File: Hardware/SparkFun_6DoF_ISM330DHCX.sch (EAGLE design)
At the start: 31 parts, among them J1 QWIIC_RIGHT_ANGLE, J2 QWIIC_RIGHT_ANGLE, U1 ISM330DHCX

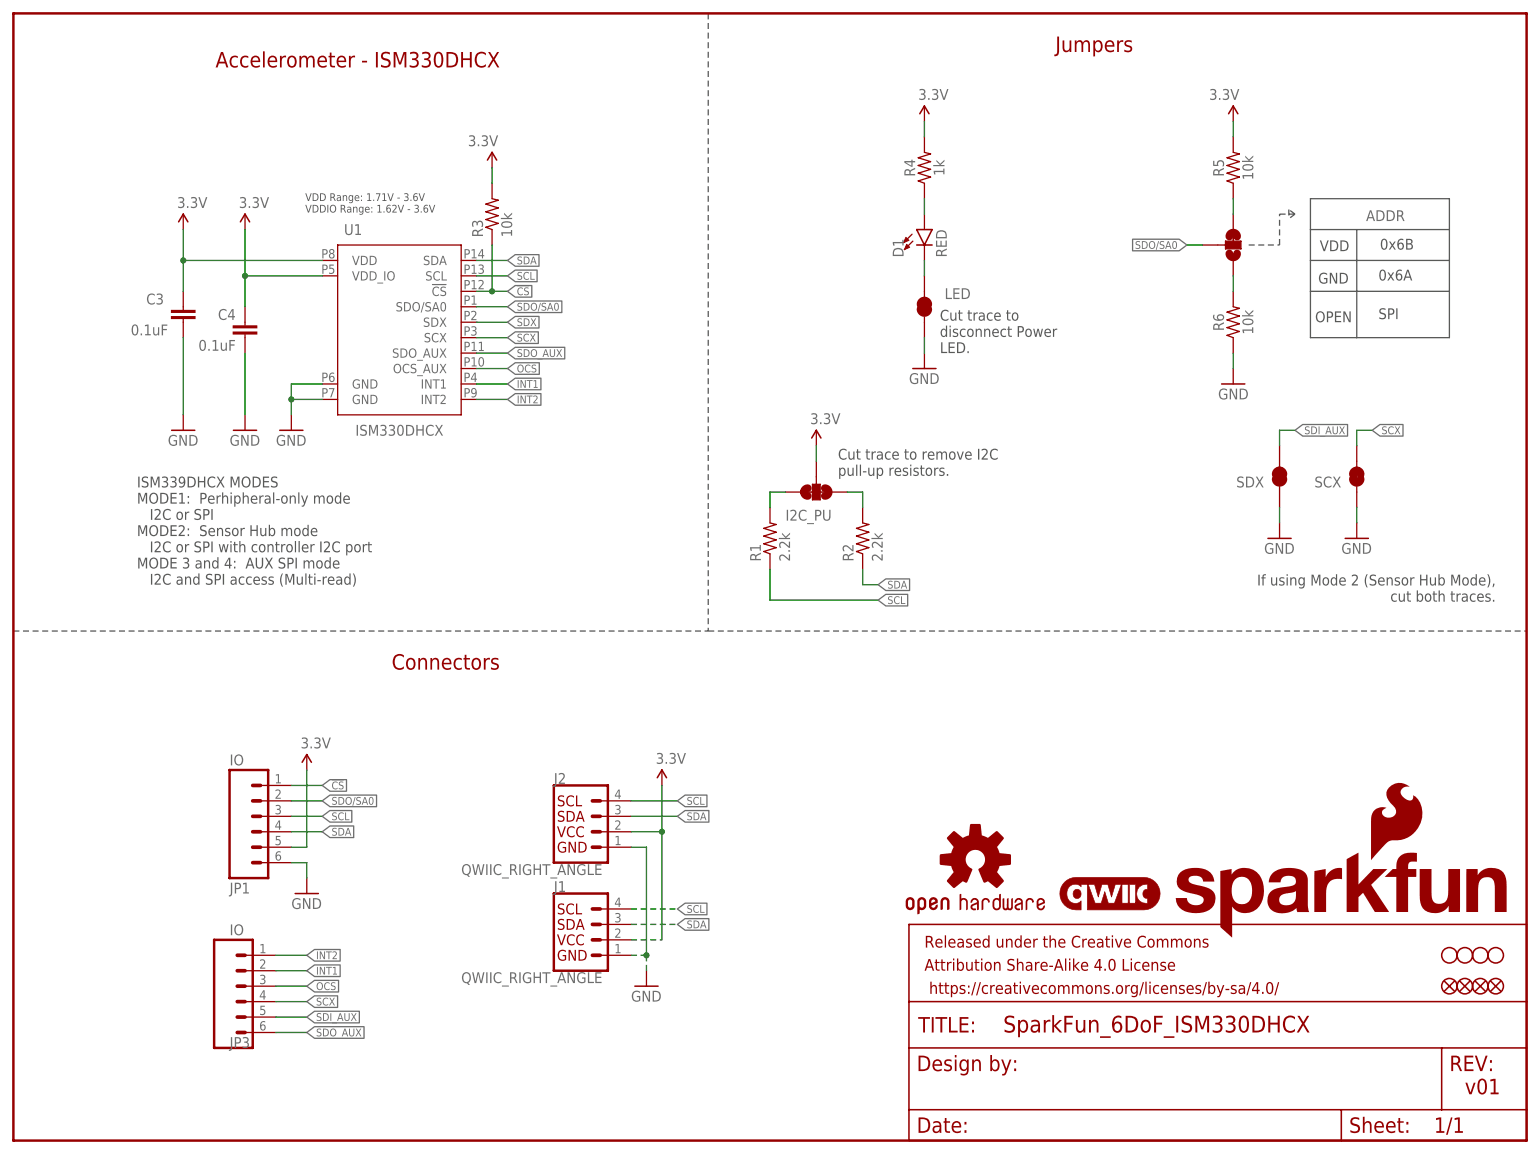
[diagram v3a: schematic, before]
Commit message: Completes routing, had to swap SDO and CS for ease of routing
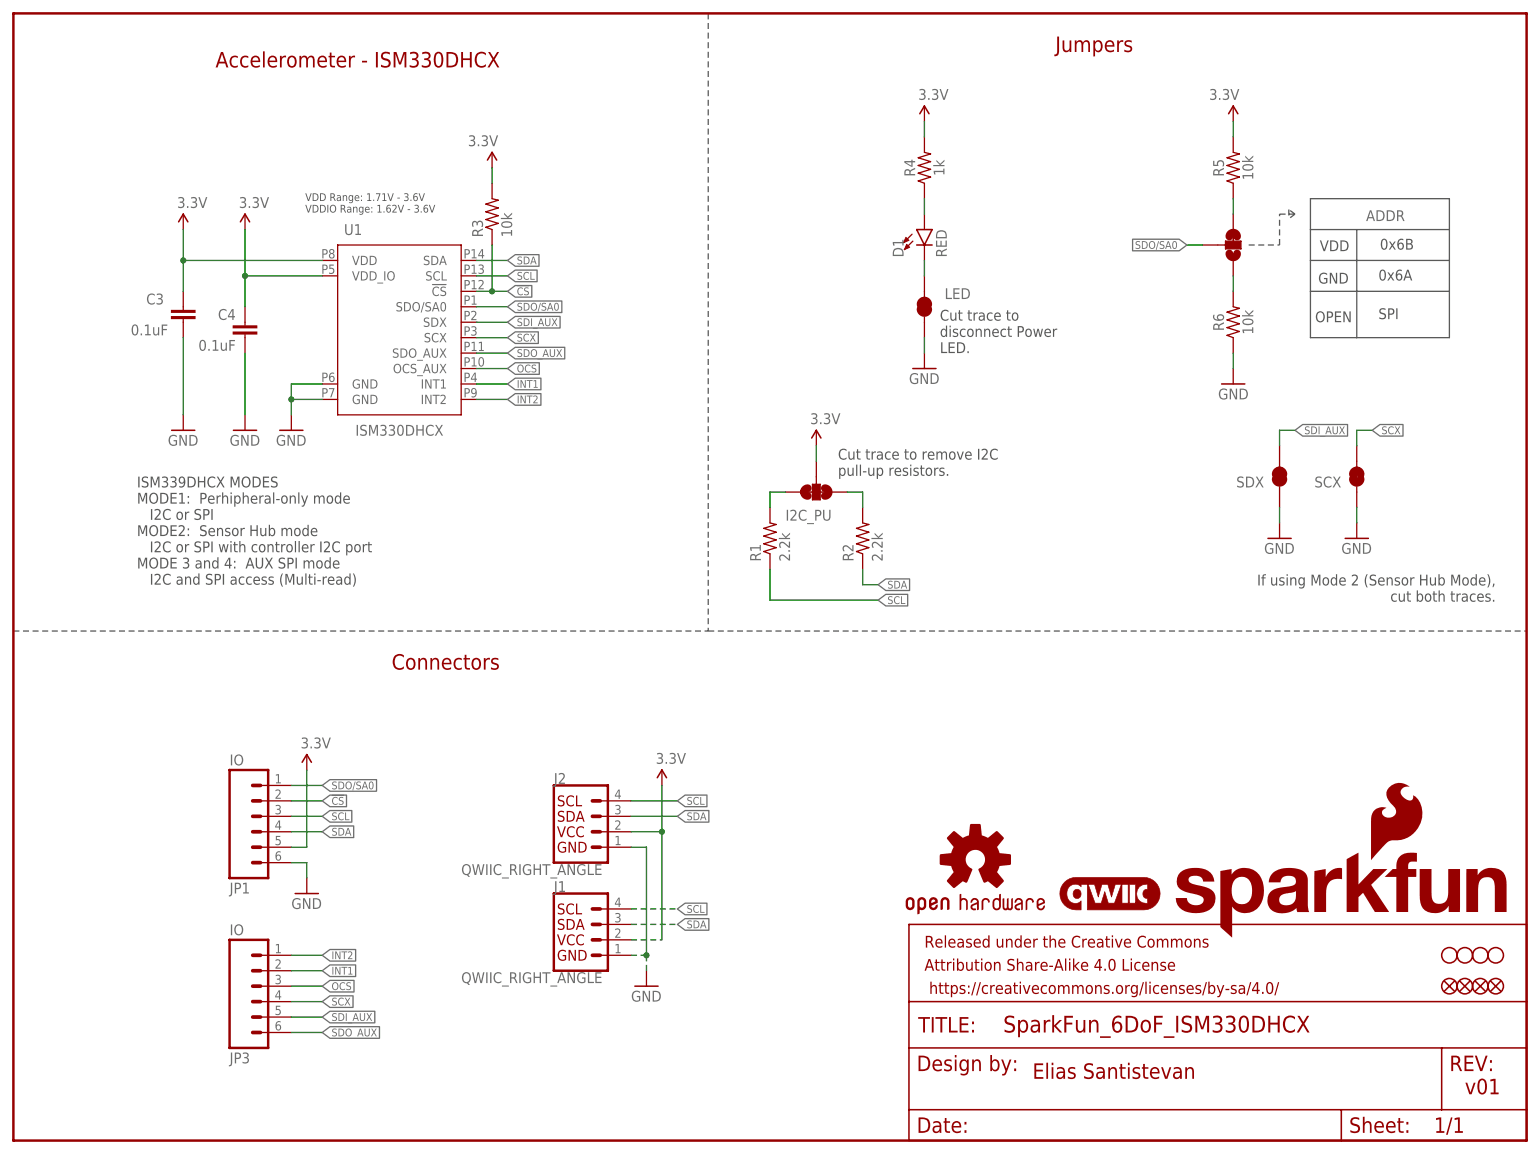
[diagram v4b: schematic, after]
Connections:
- removed net N$4: C3.1, U1.VDD
- removed net SDX: U1.SDX
- net !CS!: now also JP1.2; no longer JP1.1
- net 3.3V: now also C3.1, U1.VDD
- net SDI_AUX: now also U1.SDX
- net SDO/SA0: now also JP1.1; no longer JP1.2
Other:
- note added: "Elias Santistevan"
- moved on the sheet: JP3
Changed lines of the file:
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@@
 <wire x1="209.804" y1="153.162" x2="209.804" y2="151.638" width="0.2032" layer="97" style="dashdot"/>
 <wire x1="210.82" y1="152.4" x2="209.804" y2="151.638" width="0.2032" layer="97" style="dashdot"/>
+<text x="167.64" y="10.16" size="2.54" layer="94" font="vector">Elias Santistevan</text>
 </plain>
 <instances>
@@
 </instance>
 <instance part="LOGO3" gate="G$1" x="190.5" y="33.02" smashed="yes"/>
-<instance part="JP3" gate="G$1" x="38.1" y="25.4" smashed="yes" rot="MR180">
+<instance part="JP3" gate="G$1" x="40.64" y="25.4" smashed="yes" rot="MR180">
 <attribute name="VALUE" x="35.56" y="35.56" size="1.778" layer="96" font="vector" rot="MR180"/>
-<attribute name="NAME" x="35.56" y="17.018" size="1.778" layer="95" font="vector" rot="MR180"/>
+<attribute name="NAME" x="35.56" y="14.478" size="1.778" layer="95" font="vector" rot="MR180"/>
 </instance>
 <instance part="J1" gate="G$1" x="93.98" y="33.02" smashed="yes">
@@
 </segment>
 <segment>
-<pinref part="JP1" gate="G$1" pin="1"/>
-<wire x1="45.72" y1="58.42" x2="50.8" y2="58.42" width="0.1524" layer="91"/>
-<label x="50.8" y="58.42" size="1.27" layer="95" font="vector" xref="yes"/>
-</segment>
-</net>
-<net name="SDO/SA0" class="0">
-<segment>
-<pinref part="JP1" gate="G$1" pin="2"/>
 <wire x1="45.72" y1="55.88" x2="50.8" y2="55.88" width="0.1524" layer="91"/>
 <label x="50.8" y="55.88" size="1.27" layer="95" font="vector" xref="yes"/>
-</segment>
+<pinref part="JP1" gate="G$1" pin="2"/>
+</segment>
+</net>
+<net name="SDO/SA0" class="0">
 <segment>
 <wire x1="76.2" y1="137.16" x2="81.28" y2="137.16" width="0.1524" layer="91"/>
@@
 <label x="193.04" y="147.32" size="1.27" layer="95" font="vector" rot="R180" xref="yes"/>
 </segment>
+<segment>
+<wire x1="45.72" y1="58.42" x2="50.8" y2="58.42" width="0.1524" layer="91"/>
+<label x="50.8" y="58.42" size="1.27" layer="95" font="vector" xref="yes"/>
+<pinref part="JP1" gate="G$1" pin="1"/>
+</segment>
 </net>
 <net name="SDI_AUX" class="0">
 <segment>
 <pinref part="JP3" gate="G$1" pin="5"/>
-<wire x1="43.18" y1="20.32" x2="48.26" y2="20.32" width="0.1524" layer="91"/>
-<label x="48.26" y="20.32" size="1.27" layer="95" font="vector" xref="yes"/>
+<wire x1="45.72" y1="20.32" x2="50.8" y2="20.32" width="0.1524" layer="91"/>
+<label x="50.8" y="20.32" size="1.27" layer="95" font="vector" xref="yes"/>
 </segment>
 <segment>
@@
 <label x="210.82" y="116.84" size="1.27" layer="95" font="vector" xref="yes"/>
 </segment>
+<segment>
+<wire x1="76.2" y1="134.62" x2="81.28" y2="134.62" width="0.1524" layer="91"/>
+<label x="81.28" y="134.62" size="1.27" layer="95" font="vector" xref="yes"/>
+<pinref part="U1" gate="G$1" pin="SDX"/>
+</segment>
 </net>
 <net name="SCX" class="0">
 <segment>
 <pinref part="JP3" gate="G$1" pin="4"/>
-<wire x1="43.18" y1="22.86" x2="48.26" y2="22.86" width="0.1524" layer="91"/>
-<label x="48.26" y="22.86" size="1.27" layer="95" font="vector" xref="yes"/>
+<wire x1="45.72" y1="22.86" x2="50.8" y2="22.86" width="0.1524" layer="91"/>
+<label x="50.8" y="22.86" size="1.27" layer="95" font="vector" xref="yes"/>
 </segment>
 <segment>
@@
 <segment>
 <pinref part="JP3" gate="G$1" pin="2"/>
-<wire x1="43.18" y1="27.94" x2="48.26" y2="27.94" width="0.1524" layer="91"/>
-<label x="48.26" y="27.94" size="1.27" layer="95" font="vector" xref="yes"/>
+<wire x1="45.72" y1="27.94" x2="50.8" y2="27.94" width="0.1524" layer="91"/>
+<label x="50.8" y="27.94" size="1.27" layer="95" font="vector" xref="yes"/>
 </segment>
 </net>
@@
 <segment>
 <pinref part="JP3" gate="G$1" pin="1"/>
-<wire x1="43.18" y1="30.48" x2="48.26" y2="30.48" width="0.1524" layer="91"/>
-<label x="48.26" y="30.48" size="1.27" layer="95" font="vector" xref="yes"/>
+<wire x1="45.72" y1="30.48" x2="50.8" y2="30.48" width="0.1524" layer="91"/>
+<label x="50.8" y="30.48" size="1.27" layer="95" font="vector" xref="yes"/>
 </segment>
 <segment>
@@
 <wire x1="200.66" y1="167.64" x2="200.66" y2="165.1" width="0.1524" layer="91"/>
 </segment>
+<segment>
+<pinref part="C3" gate="G$1" pin="1"/>
+<wire x1="27.94" y1="139.7" x2="27.94" y2="144.78" width="0.1524" layer="91"/>
+<wire x1="27.94" y1="144.78" x2="50.8" y2="144.78" width="0.1524" layer="91"/>
+<pinref part="U1" gate="G$1" pin="VDD"/>
+<pinref part="SUPPLY5" gate="G$1" pin="3.3V"/>
+<wire x1="27.94" y1="149.86" x2="27.94" y2="144.78" width="0.1524" layer="91"/>
+<junction x="27.94" y="144.78"/>
+</segment>
 </net>
 <net name="OCS" class="0">
@@
 <segment>
 <pinref part="JP3" gate="G$1" pin="3"/>
-<wire x1="43.18" y1="25.4" x2="48.26" y2="25.4" width="0.1524" layer="91"/>
-<label x="48.26" y="25.4" size="1.27" layer="95" font="vector" xref="yes"/>
+<wire x1="45.72" y1="25.4" x2="50.8" y2="25.4" width="0.1524" layer="91"/>
+<label x="50.8" y="25.4" size="1.27" layer="95" font="vector" xref="yes"/>
 </segment>
 </net>
@@
 <segment>
 <pinref part="JP3" gate="G$1" pin="6"/>
-<wire x1="43.18" y1="17.78" x2="48.26" y2="17.78" width="0.1524" layer="91"/>
-<label x="48.26" y="17.78" size="1.27" layer="95" xref="yes"/>
-</segment>
-</net>
-<net name="SDX" class="0">
-<segment>
-<wire x1="76.2" y1="134.62" x2="81.28" y2="134.62" width="0.1524" layer="91"/>
-<label x="81.28" y="134.62" size="1.27" layer="95" font="vector" xref="yes"/>
-<pinref part="U1" gate="G$1" pin="SDX"/>
-</segment>
-</net>
-<net name="N$4" class="0">
-<segment>
-<pinref part="C3" gate="G$1" pin="1"/>
-<wire x1="27.94" y1="139.7" x2="27.94" y2="144.78" width="0.1524" layer="91"/>
-<wire x1="27.94" y1="144.78" x2="50.8" y2="144.78" width="0.1524" layer="91"/>
-<pinref part="SUPPLY5" gate="G$1" pin="3.3V"/>
-<wire x1="27.94" y1="149.86" x2="27.94" y2="144.78" width="0.1524" layer="91"/>
-<junction x="27.94" y="144.78"/>
-<pinref part="U1" gate="G$1" pin="VDD"/>
+<wire x1="45.72" y1="17.78" x2="50.8" y2="17.78" width="0.1524" layer="91"/>
+<label x="50.8" y="17.78" size="1.27" layer="95" xref="yes"/>
 </segment>
 </net>
@@
 </sheet>
 </sheets>
-<errors>
-</errors>
 </schematic>
 </drawing>
